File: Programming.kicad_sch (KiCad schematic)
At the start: 0 parts

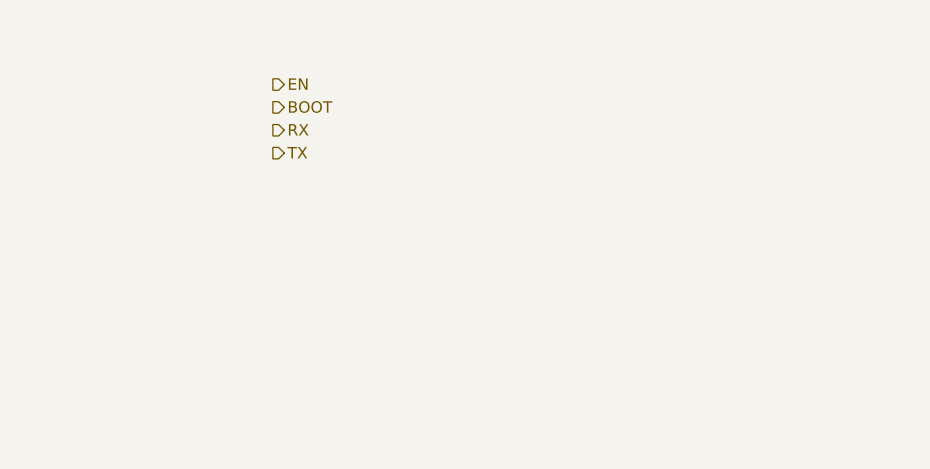
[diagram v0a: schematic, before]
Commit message: working on ignition and power output sheets
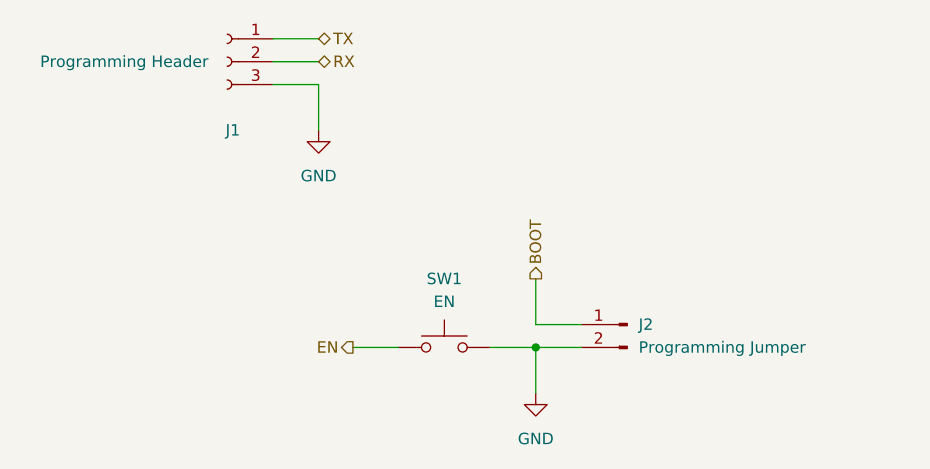
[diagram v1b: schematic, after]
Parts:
- added J1: Programming Header, Connector_PinHeader_2.54mm:PinHeader_1x03_P2.54mm_Horizontal, symbol Connector:Conn_01x03_Socket
- added J2: Programming Jumper, Connector_PinHeader_2.54mm:PinHeader_1x02_P2.54mm_Horizontal, symbol Connector:Conn_01x02_Pin
- added SW1: EN, Button_Switch_SMD:SW_SPST_TL3305B, symbol Switch:SW_Push
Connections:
- net BOOT: now also J2.1 (Pin_1)
- net EN: now also SW1.2
- net RX: now also J1.2 (Pin_2)
- net TX: now also J1.1 (Pin_1)
- new net GND: J1.3 (Pin_3), J2.2 (Pin_2), SW1.1
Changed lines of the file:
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@@
     (date "2023-11-22")
   )
-  (hierarchical_label "BOOT" (shape output) (at 127 91.44 0) (fields_autoplaced)
+  (junction (at 156.21 118.11) (diameter 0) (color 0 0 0 0)
+  )
+  (wire (pts (xy 140.97 118.11) (xy 135.89 118.11))
+    (stroke (width 0) (type default))
+  )
+  (wire (pts (xy 127 86.36) (xy 132.08 86.36))
+    (stroke (width 0) (type default))
+  )
+  (wire (pts (xy 161.29 118.11) (xy 156.21 118.11))
+    (stroke (width 0) (type default))
+  )
+  (wire (pts (xy 151.13 118.11) (xy 156.21 118.11))
+    (stroke (width 0) (type default))
+  )
+  (wire (pts (xy 156.21 110.49) (xy 156.21 115.57))
+    (stroke (width 0) (type default))
+  )
+  (wire (pts (xy 127 88.9) (xy 132.08 88.9))
+    (stroke (width 0) (type default))
+  )
+  (wire (pts (xy 132.08 88.9) (xy 132.08 93.98))
+    (stroke (width 0) (type default))
+  )
+  (wire (pts (xy 156.21 118.11) (xy 156.21 123.19))
+    (stroke (width 0) (type default))
+  )
+  (wire (pts (xy 127 83.82) (xy 132.08 83.82))
+    (stroke (width 0) (type default))
+  )
+  (wire (pts (xy 156.21 115.57) (xy 161.29 115.57))
+    (stroke (width 0) (type default))
+  )
+  (hierarchical_label "EN" (shape output) (at 135.89 118.11 180) (fields_autoplaced)
+    (effects (font (size 1.27 1.27)) (justify right))
+  )
+  (hierarchical_label "BOOT" (shape output) (at 156.21 110.49 90) (fields_autoplaced)
     (effects (font (size 1.27 1.27)) (justify left))
   )
-  (hierarchical_label "EN" (shape output) (at 127 88.9 0) (fields_autoplaced)
+  (hierarchical_label "TX" (shape bidirectional) (at 132.08 83.82 0) (fields_autoplaced)
     (effects (font (size 1.27 1.27)) (justify left))
   )
-  (hierarchical_label "RX" (shape output) (at 127 93.98 0) (fields_autoplaced)
+  (hierarchical_label "RX" (shape bidirectional) (at 132.08 86.36 0) (fields_autoplaced)
     (effects (font (size 1.27 1.27)) (justify left))
   )
-  (hierarchical_label "TX" (shape output) (at 127 96.52 0) (fields_autoplaced)
-    (effects (font (size 1.27 1.27)) (justify left))
+  (symbol (lib_id "Connector:Conn_01x03_Socket") (at 121.92 86.36 0) (mirror y) (unit 1)
+    (in_bom no) (on_board yes) (dnp no)
+    (property "Reference" "J1" (at 122.555 93.98 0)
+      (effects (font (size 1.27 1.27)))
+    )
+    (property "Value" "Programming Header" (at 110.49 86.36 0)
+      (effects (font (size 1.27 1.27)))
+    )
+    (property "Footprint" "Connector_PinHeader_2.54mm:PinHeader_1x03_P2.54mm_Horizontal" (at 121.92 86.36 0)
+      (effects (font (size 1.27 1.27)) hide)
+    )
+    (property "Datasheet" "~" (at 121.92 86.36 0)
+      (effects (font (size 1.27 1.27)) hide)
+    )
+    (pin "1")
+    (pin "2")
+    (pin "3")
+    (instances
+      (project "control-module-pcb"
+        (path "/4c946e98-79c2-4a2d-bd7f-2a33db8d8c91/689f1063-70bb-4257-9aa2-434555b9eee7"
+          (reference "J1") (unit 1)
+        )
+      )
+      (project "key-fob-pcb"
+        (path "/b002c3bf-fc58-4993-80f7-7914d3aa1ac9/a04b704b-7ebc-4a7f-8071-91aed1728ce2"
+          (reference "J2") (unit 1)
+        )
+      )
+    )
+  )
+  (symbol (lib_id "power:GND") (at 132.08 93.98 0) (unit 1)
+    (in_bom yes) (on_board yes) (dnp no) (fields_autoplaced)
+    (property "Reference" "#PWR015" (at 132.08 100.33 0)
+      (effects (font (size 1.27 1.27)) hide)
+    )
+    (property "Value" "GND" (at 132.08 99.06 0)
+      (effects (font (size 1.27 1.27)))
+    )
+    (property "Footprint" "" (at 132.08 93.98 0)
+      (effects (font (size 1.27 1.27)) hide)
+    )
+    (property "Datasheet" "" (at 132.08 93.98 0)
+      (effects (font (size 1.27 1.27)) hide)
+    )
+    (pin "1")
+    (instances
+      (project "control-module-pcb"
+        (path "/4c946e98-79c2-4a2d-bd7f-2a33db8d8c91/689f1063-70bb-4257-9aa2-434555b9eee7"
+          (reference "#PWR015") (unit 1)
+        )
+      )
+    )
+  )
+  (symbol (lib_id "Connector:Conn_01x02_Pin") (at 166.37 115.57 0) (mirror y) (unit 1)
+    (in_bom no) (on_board yes) (dnp no) (fields_autoplaced)
+    (property "Reference" "J2" (at 167.64 115.57 0)
+      (effects (font (size 1.27 1.27)) (justify right))
+    )
+    (property "Value" "Programming Jumper" (at 167.64 118.11 0)
+      (effects (font (size 1.27 1.27)) (justify right))
+    )
+    (property "Footprint" "Connector_PinHeader_2.54mm:PinHeader_1x02_P2.54mm_Horizontal" (at 166.37 115.57 0)
+      (effects (font (size 1.27 1.27)) hide)
+    )
+    (property "Datasheet" "~" (at 166.37 115.57 0)
+      (effects (font (size 1.27 1.27)) hide)
+    )
+    (pin "1")
+    (pin "2")
+    (instances
+      (project "control-module-pcb"
+        (path "/4c946e98-79c2-4a2d-bd7f-2a33db8d8c91/689f1063-70bb-4257-9aa2-434555b9eee7"
+          (reference "J2") (unit 1)
+        )
+      )
+      (project "key-fob-pcb"
+        (path "/b002c3bf-fc58-4993-80f7-7914d3aa1ac9/a04b704b-7ebc-4a7f-8071-91aed1728ce2"
+          (reference "J1") (unit 1)
+        )
+      )
+    )
+  )
+  (symbol (lib_id "power:GND") (at 156.21 123.19 0) (unit 1)
+    (in_bom yes) (on_board yes) (dnp no) (fields_autoplaced)
+    (property "Reference" "#PWR016" (at 156.21 129.54 0)
+      (effects (font (size 1.27 1.27)) hide)
+    )
+    (property "Value" "GND" (at 156.21 128.27 0)
+      (effects (font (size 1.27 1.27)))
+    )
+    (property "Footprint" "" (at 156.21 123.19 0)
+      (effects (font (size 1.27 1.27)) hide)
+    )
+    (property "Datasheet" "" (at 156.21 123.19 0)
+      (effects (font (size 1.27 1.27)) hide)
+    )
+    (pin "1")
+    (instances
+      (project "control-module-pcb"
+        (path "/4c946e98-79c2-4a2d-bd7f-2a33db8d8c91/689f1063-70bb-4257-9aa2-434555b9eee7"
+          (reference "#PWR016") (unit 1)
+        )
+      )
+    )
+  )
+  (symbol (lib_id "Switch:SW_Push") (at 146.05 118.11 0) (mirror y) (unit 1)
+    (in_bom no) (on_board yes) (dnp no)
+    (property "Reference" "SW1" (at 146.05 110.49 0)
+      (effects (font (size 1.27 1.27)))
+    )
+    (property "Value" "EN" (at 146.05 113.03 0)
+      (effects (font (size 1.27 1.27)))
+    )
+    (property "Footprint" "Button_Switch_SMD:SW_SPST_TL3305B" (at 146.05 113.03 0)
+      (effects (font (size 1.27 1.27)) hide)
+    )
+    (property "Datasheet" "~" (at 146.05 113.03 0)
+      (effects (font (size 1.27 1.27)) hide)
+    )
+    (pin "1")
+    (pin "2")
+    (instances
+      (project "control-module-pcb"
+        (path "/4c946e98-79c2-4a2d-bd7f-2a33db8d8c91/689f1063-70bb-4257-9aa2-434555b9eee7"
+          (reference "SW1") (unit 1)
+        )
+      )
+      (project "key-fob-pcb"
+        (path "/b002c3bf-fc58-4993-80f7-7914d3aa1ac9/2e0921b6-f0d9-4f19-880e-02dc034cc8b0"
+          (reference "SW4") (unit 1)
+        )
+        (path "/b002c3bf-fc58-4993-80f7-7914d3aa1ac9/a04b704b-7ebc-4a7f-8071-91aed1728ce2"
+          (reference "SW2") (unit 1)
+        )
+      )
+    )
   )
 )

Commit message: switch Ignition page to use load drivers rather than discrete FETs
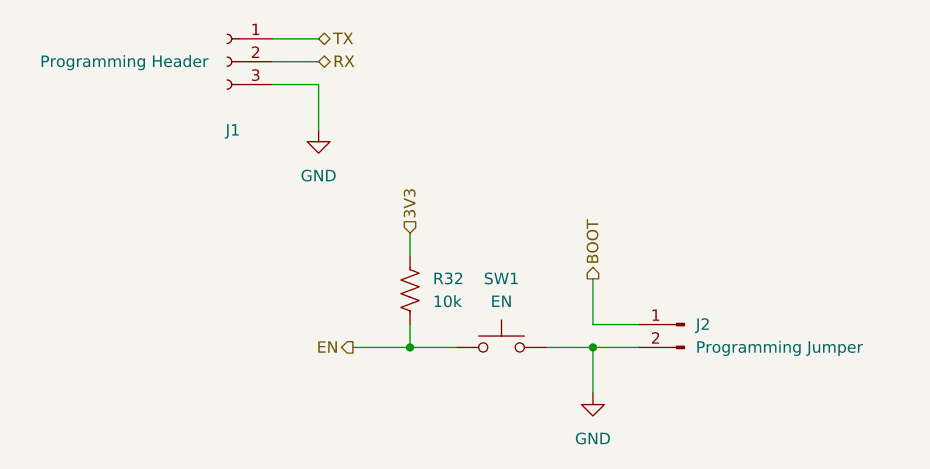
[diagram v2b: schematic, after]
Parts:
- added R32: 10k, symbol Device:R_US
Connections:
- net EN: now also R32.2
- new net 3V3: R32.1
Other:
- company: (none) -> J2B
- moved on the sheet: J2, SW1
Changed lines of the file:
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@@
     (title "Control Module")
     (date "2023-11-22")
-  )
-  (junction (at 156.21 118.11) (diameter 0) (color 0 0 0 0)
-  )
-  (wire (pts (xy 140.97 118.11) (xy 135.89 118.11))
+    (company "J2B")
+    (comment 1 "Author: Ben Martens")
+  )
+  (junction (at 142.24 118.11) (diameter 0) (color 0 0 0 0)
+  )
+  (junction (at 162.56 118.11) (diameter 0) (color 0 0 0 0)
+  )
+  (wire (pts (xy 147.32 118.11) (xy 142.24 118.11))
+    (stroke (width 0) (type default))
+  )
+  (wire (pts (xy 142.24 118.11) (xy 135.89 118.11))
     (stroke (width 0) (type default))
   )
@@
     (stroke (width 0) (type default))
   )
-  (wire (pts (xy 161.29 118.11) (xy 156.21 118.11))
-    (stroke (width 0) (type default))
-  )
-  (wire (pts (xy 151.13 118.11) (xy 156.21 118.11))
-    (stroke (width 0) (type default))
-  )
-  (wire (pts (xy 156.21 110.49) (xy 156.21 115.57))
+  (wire (pts (xy 167.64 118.11) (xy 162.56 118.11))
+    (stroke (width 0) (type default))
+  )
+  (wire (pts (xy 157.48 118.11) (xy 162.56 118.11))
+    (stroke (width 0) (type default))
+  )
+  (wire (pts (xy 162.56 110.49) (xy 162.56 115.57))
     (stroke (width 0) (type default))
   )
@@
     (stroke (width 0) (type default))
   )
+  (wire (pts (xy 142.24 115.57) (xy 142.24 118.11))
+    (stroke (width 0) (type default))
+  )
   (wire (pts (xy 132.08 88.9) (xy 132.08 93.98))
     (stroke (width 0) (type default))
   )
-  (wire (pts (xy 156.21 118.11) (xy 156.21 123.19))
+  (wire (pts (xy 162.56 118.11) (xy 162.56 123.19))
+    (stroke (width 0) (type default))
+  )
+  (wire (pts (xy 142.24 105.41) (xy 142.24 107.95))
     (stroke (width 0) (type default))
   )
@@
     (stroke (width 0) (type default))
   )
-  (wire (pts (xy 156.21 115.57) (xy 161.29 115.57))
+  (wire (pts (xy 162.56 115.57) (xy 167.64 115.57))
     (stroke (width 0) (type default))
   )
@@
     (effects (font (size 1.27 1.27)) (justify right))
   )
-  (hierarchical_label "BOOT" (shape output) (at 156.21 110.49 90) (fields_autoplaced)
+  (hierarchical_label "BOOT" (shape output) (at 162.56 110.49 90) (fields_autoplaced)
     (effects (font (size 1.27 1.27)) (justify left))
   )
@@
   )
   (hierarchical_label "RX" (shape bidirectional) (at 132.08 86.36 0) (fields_autoplaced)
+    (effects (font (size 1.27 1.27)) (justify left))
+  )
+  (hierarchical_label "3V3" (shape input) (at 142.24 105.41 90) (fields_autoplaced)
     (effects (font (size 1.27 1.27)) (justify left))
   )
@@
     )
   )
-  (symbol (lib_id "Connector:Conn_01x02_Pin") (at 166.37 115.57 0) (mirror y) (unit 1)
+  (symbol (lib_id "Connector:Conn_01x02_Pin") (at 172.72 115.57 0) (mirror y) (unit 1)
     (in_bom no) (on_board yes) (dnp no) (fields_autoplaced)
-    (property "Reference" "J2" (at 167.64 115.57 0)
+    (property "Reference" "J2" (at 173.99 115.57 0)
       (effects (font (size 1.27 1.27)) (justify right))
     )
-    (property "Value" "Programming Jumper" (at 167.64 118.11 0)
+    (property "Value" "Programming Jumper" (at 173.99 118.11 0)
       (effects (font (size 1.27 1.27)) (justify right))
     )
-    (property "Footprint" "Connector_PinHeader_2.54mm:PinHeader_1x02_P2.54mm_Horizontal" (at 166.37 115.57 0)
-      (effects (font (size 1.27 1.27)) hide)
-    )
-    (property "Datasheet" "~" (at 166.37 115.57 0)
+    (property "Footprint" "Connector_PinHeader_2.54mm:PinHeader_1x02_P2.54mm_Horizontal" (at 172.72 115.57 0)
+      (effects (font (size 1.27 1.27)) hide)
+    )
+    (property "Datasheet" "~" (at 172.72 115.57 0)
       (effects (font (size 1.27 1.27)) hide)
     )
@@
     )
   )
-  (symbol (lib_id "power:GND") (at 156.21 123.19 0) (unit 1)
+  (symbol (lib_id "power:GND") (at 162.56 123.19 0) (unit 1)
     (in_bom yes) (on_board yes) (dnp no) (fields_autoplaced)
-    (property "Reference" "#PWR016" (at 156.21 129.54 0)
-      (effects (font (size 1.27 1.27)) hide)
-    )
-    (property "Value" "GND" (at 156.21 128.27 0)
-      (effects (font (size 1.27 1.27)))
-    )
-    (property "Footprint" "" (at 156.21 123.19 0)
-      (effects (font (size 1.27 1.27)) hide)
-    )
-    (property "Datasheet" "" (at 156.21 123.19 0)
+    (property "Reference" "#PWR016" (at 162.56 129.54 0)
+      (effects (font (size 1.27 1.27)) hide)
+    )
+    (property "Value" "GND" (at 162.56 128.27 0)
+      (effects (font (size 1.27 1.27)))
+    )
+    (property "Footprint" "" (at 162.56 123.19 0)
+      (effects (font (size 1.27 1.27)) hide)
+    )
+    (property "Datasheet" "" (at 162.56 123.19 0)
       (effects (font (size 1.27 1.27)) hide)
     )
@@
     )
   )
-  (symbol (lib_id "Switch:SW_Push") (at 146.05 118.11 0) (mirror y) (unit 1)
+  (symbol (lib_id "Device:R_US") (at 142.24 111.76 0) (unit 1)
+    (in_bom yes) (on_board yes) (dnp no) (fields_autoplaced)
+    (property "Reference" "R32" (at 144.78 110.49 0)
+      (effects (font (size 1.27 1.27)) (justify left))
+    )
+    (property "Value" "10k" (at 144.78 113.03 0)
+      (effects (font (size 1.27 1.27)) (justify left))
+    )
+    (property "Footprint" "" (at 143.256 112.014 90)
+      (effects (font (size 1.27 1.27)) hide)
+    )
+    (property "Datasheet" "~" (at 142.24 111.76 0)
+      (effects (font (size 1.27 1.27)) hide)
+    )
+    (pin "1")
+    (pin "2")
+    (instances
+      (project "control-module-pcb"
+        (path "/4c946e98-79c2-4a2d-bd7f-2a33db8d8c91/689f1063-70bb-4257-9aa2-434555b9eee7"
+          (reference "R32") (unit 1)
+        )
+      )
+    )
+  )
+  (symbol (lib_id "Switch:SW_Push") (at 152.4 118.11 0) (mirror y) (unit 1)
     (in_bom no) (on_board yes) (dnp no)
-    (property "Reference" "SW1" (at 146.05 110.49 0)
-      (effects (font (size 1.27 1.27)))
-    )
-    (property "Value" "EN" (at 146.05 113.03 0)
-      (effects (font (size 1.27 1.27)))
-    )
-    (property "Footprint" "Button_Switch_SMD:SW_SPST_TL3305B" (at 146.05 113.03 0)
-      (effects (font (size 1.27 1.27)) hide)
-    )
-    (property "Datasheet" "~" (at 146.05 113.03 0)
-      (effects (font (size 1.27 1.27)) hide)
-    )
+    (property "Reference" "SW1" (at 152.4 110.49 0)
+      (effects (font (size 1.27 1.27)))
+    )
+    (property "Value" "EN" (at 152.4 113.03 0)
+      (effects (font (size 1.27 1.27)))
+    )
+    (property "Footprint" "Button_Switch_SMD:SW_SPST_TL3305B" (at 152.4 113.03 0)
+      (effects (font (size 1.27 1.27)) hide)
+    )
+    (property "Datasheet" "~" (at 152.4 113.03 0)
+      (effects (font (size 1.27 1.27)) hide)
+    )

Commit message: Assigning footprints
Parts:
- R32: footprint (none) -> Resistor_SMD:R_0603_1608Metric
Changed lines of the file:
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@@
       (effects (font (size 1.27 1.27)) (justify left))
     )
-    (property "Footprint" "" (at 143.256 112.014 90)
+    (property "Footprint" "Resistor_SMD:R_0603_1608Metric" (at 143.256 112.014 90)
       (effects (font (size 1.27 1.27)) hide)
     )

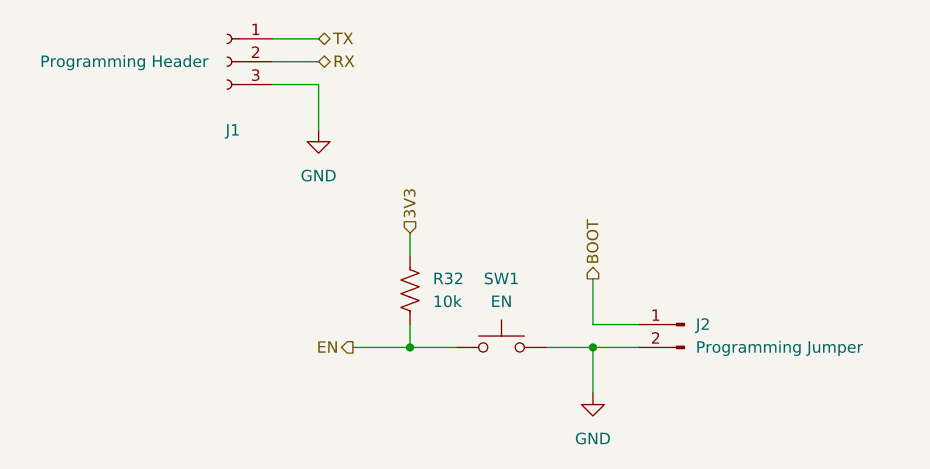
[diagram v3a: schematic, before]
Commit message: finished assigning footprints and started PCB layout
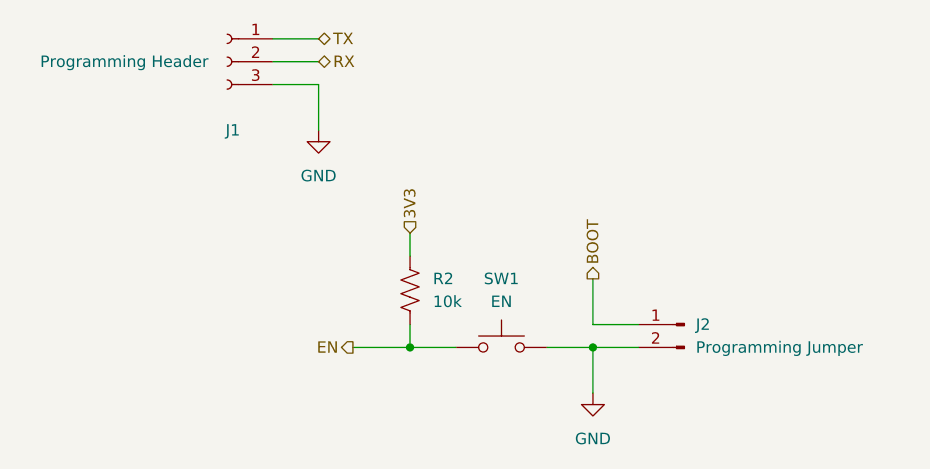
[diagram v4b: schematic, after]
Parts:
- renumbered R32 to R2
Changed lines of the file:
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@@
   (symbol (lib_id "Device:R_US") (at 142.24 111.76 0) (unit 1)
     (in_bom yes) (on_board yes) (dnp no) (fields_autoplaced)
-    (property "Reference" "R32" (at 144.78 110.49 0)
+    (property "Reference" "R2" (at 144.78 110.49 0)
       (effects (font (size 1.27 1.27)) (justify left))
     )
@@
       (project "control-module-pcb"
         (path "/4c946e98-79c2-4a2d-bd7f-2a33db8d8c91/689f1063-70bb-4257-9aa2-434555b9eee7"
-          (reference "R32") (unit 1)
+          (reference "R2") (unit 1)
         )
       )
